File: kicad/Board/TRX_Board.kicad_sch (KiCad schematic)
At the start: 60 parts, among them J1 Conn_02x08_Odd_Even, J2 SMA, J3 Conn_01x03, J4 Conn_01x03, Q1 BSN20, Q2 BSN20, Q3 BSN20, U1 AP1117-33, U2 LM386, U3 DRA818U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

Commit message: Changed page information
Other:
- company: (none) -> digitalwire.ch
- title: (none) -> VHF-UHF TRX-Board
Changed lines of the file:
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@@
 (kicad_sch (version 20211123) (generator eeschema)
   (paper "A4")
+  (title_block
+    (title "VHF-UHF TRX-Board")
+    (date "2021-12-26")
+    (rev "V 1.0a")
+    (company "digitalwire.ch")
+  )
   (junction (at 205.74 72.39) (diameter 0) (color 0 0 0 0)
   )

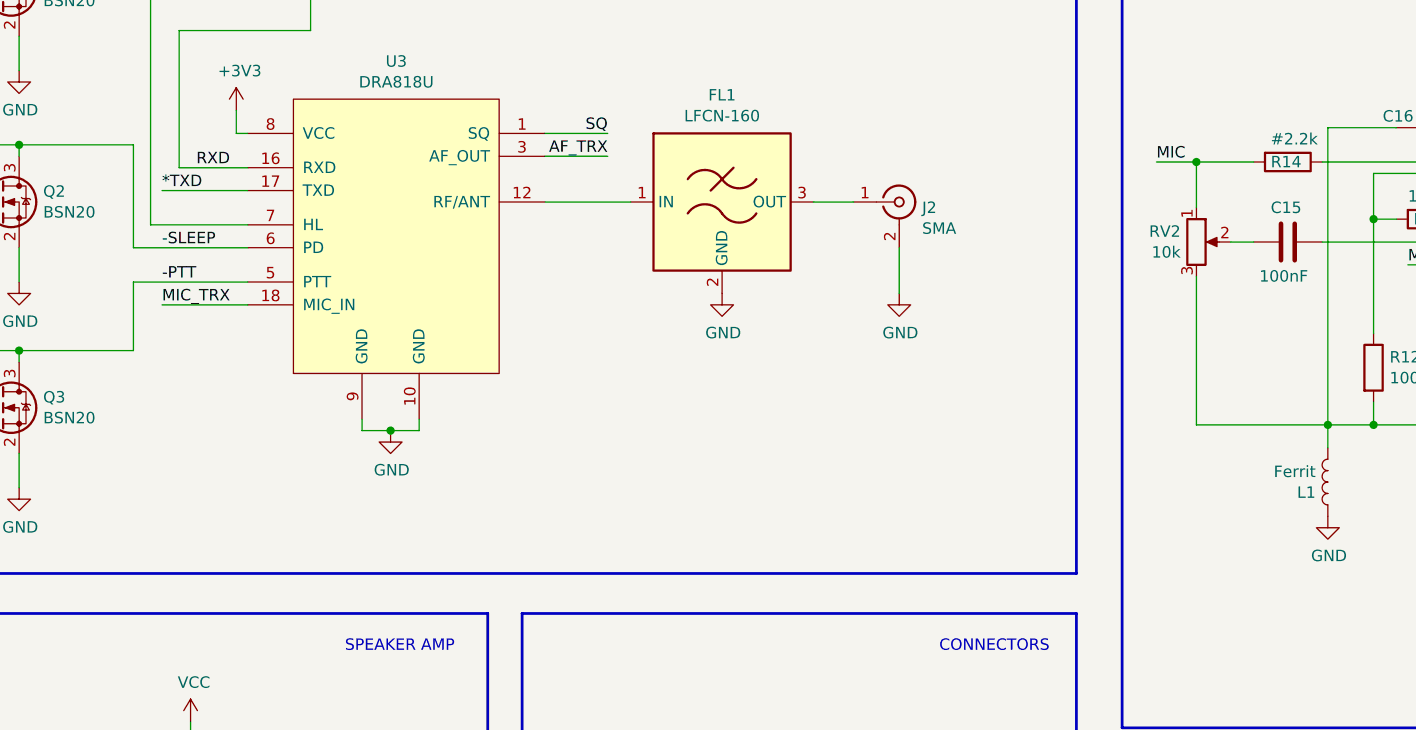
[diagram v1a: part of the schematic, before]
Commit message: Changed Mic Input
- Removed Poti near Mic
- Added Poti and jumper near the module
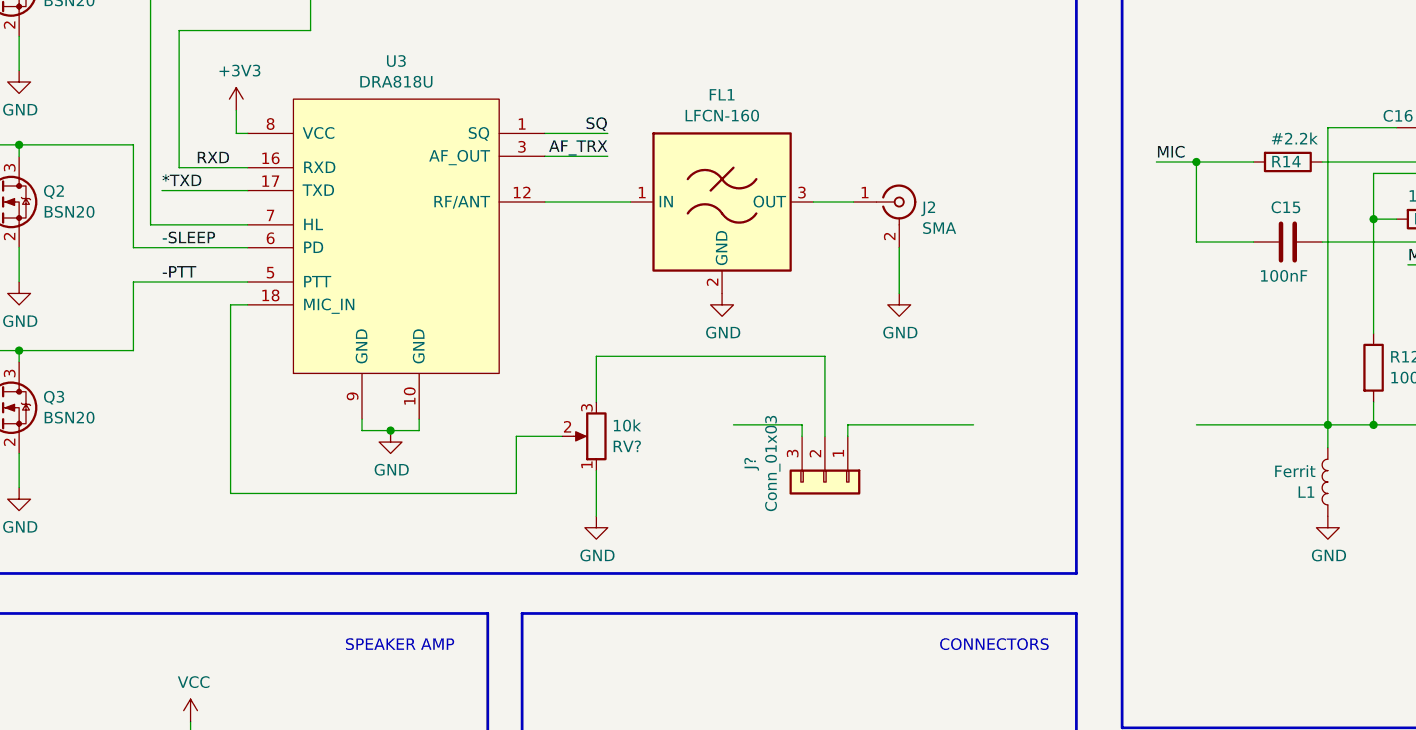
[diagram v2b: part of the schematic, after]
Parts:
- removed RV2: 10k, Potentiometer_SMD:Potentiometer_Vishay_TS53YL_Vertical, symbol Device:R_POT
- added J?: Conn_01x03, Connector_PinHeader_2.54mm:PinHeader_1x03_P2.54mm_Vertical, symbol Connector_Generic:Conn_01x03
- added RV?: 10k, Potentiometer_SMD:Potentiometer_Vishay_TS53YL_Vertical, symbol Device:R_POT
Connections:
- net GND: now also RV?.1
- net MIC: now also C15.2
- net MIC_TRX: no longer U3.18 (MIC_IN)
- new net: RV?.2, U3.18 (MIC_IN)
- new net: J?.2 (Pin_2), RV?.3
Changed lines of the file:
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@@
+    (stroke (width 0) (type default) (color 0 0 0 0))
+  )
+  (wire (pts (xy 137.16 73.66) (xy 137.16 72.39))
     (stroke (width 0) (type default) (color 0 0 0 0))
   )
@@
     (stroke (width 0) (type default) (color 0 0 0 0))
   )
+  (wire (pts (xy 68.58 59.055) (xy 68.58 80.01))
+    (stroke (width 0) (type default) (color 0 0 0 0))
+  )
   (wire (pts (xy 241.3 64.77) (xy 241.3 72.39))
+    (stroke (width 0) (type default) (color 0 0 0 0))
+  )
+  (wire (pts (xy 100.33 80.01) (xy 100.33 73.66))
     (stroke (width 0) (type default) (color 0 0 0 0))
   )
@@
     (stroke (width 0) (type default) (color 0 0 0 0))
   )
+  (wire (pts (xy 100.33 73.66) (xy 105.41 73.66))
+    (stroke (width 0) (type default) (color 0 0 0 0))
+  )
   (wire (pts (xy 70.485 46.355) (xy 60.96 46.355))
     (stroke (width 0) (type default) (color 0 0 0 0))
@@
     (stroke (width 0) (type default) (color 0 0 0 0))
   )
+  (wire (pts (xy 70.485 59.055) (xy 68.58 59.055))
+    (stroke (width 0) (type default) (color 0 0 0 0))
+  )
+  (wire (pts (xy 124.46 72.39) (xy 132.08 72.39))
+    (stroke (width 0) (type default) (color 0 0 0 0))
+  )
   (wire (pts (xy 41.275 171.45) (xy 41.275 167.005))
     (stroke (width 0) (type default) (color 0 0 0 0))
@@
   )
   (wire (pts (xy 64.135 141.605) (xy 76.835 141.605))
-    (stroke (width 0) (type default) (color 0 0 0 0))
-  )
-  (wire (pts (xy 70.485 59.055) (xy 60.96 59.055))
     (stroke (width 0) (type default) (color 0 0 0 0))
   )
@@
     (stroke (width 0.3048) (type default) (color 0 0 0 0))
   )
-  (wire (pts (xy 175.895 72.39) (xy 175.895 55.88))
-    (stroke (width 0) (type default) (color 0 0 0 0))
-  )
   (wire (pts (xy 57.785 64.135) (xy 45.085 64.135))
     (stroke (width 0) (type default) (color 0 0 0 0))
   )
-  (wire (pts (xy 179.705 52.07) (xy 182.245 52.07))
+  (wire (pts (xy 175.895 52.07) (xy 182.245 52.07))
     (stroke (width 0) (type default) (color 0 0 0 0))
   )
@@
     (stroke (width 0.3048) (type default) (color 0 0 0 0))
   )
+  (wire (pts (xy 132.08 73.66) (xy 132.08 72.39))
+    (stroke (width 0) (type default) (color 0 0 0 0))
+  )
   (wire (pts (xy 33.655 41.275) (xy 45.085 41.275))
     (stroke (width 0) (type default) (color 0 0 0 0))
   )
   (wire (pts (xy 215.9 72.39) (xy 205.74 72.39))
+    (stroke (width 0) (type default) (color 0 0 0 0))
+  )
+  (wire (pts (xy 134.62 64.77) (xy 134.62 73.66))
     (stroke (width 0) (type default) (color 0 0 0 0))
   )
@@
     (stroke (width 0.3048) (type default) (color 0 0 0 0))
   )
+  (wire (pts (xy 68.58 80.01) (xy 100.33 80.01))
+    (stroke (width 0) (type default) (color 0 0 0 0))
+  )
   (wire (pts (xy 265.43 72.39) (xy 254 72.39))
     (stroke (width 0) (type default) (color 0 0 0 0))
@@
     (stroke (width 0) (type default) (color 0 0 0 0))
   )
-  (wire (pts (xy 175.895 48.26) (xy 175.895 43.18))
+  (wire (pts (xy 175.895 43.18) (xy 175.895 52.07))
     (stroke (width 0) (type default) (color 0 0 0 0))
   )
@@
   )
   (wire (pts (xy 265.43 31.75) (xy 265.43 72.39))
+    (stroke (width 0) (type default) (color 0 0 0 0))
+  )
+  (wire (pts (xy 109.22 69.85) (xy 109.22 64.77))
     (stroke (width 0) (type default) (color 0 0 0 0))
   )
@@
     (stroke (width 0) (type default) (color 0 0 0 0))
   )
+  (wire (pts (xy 137.16 72.39) (xy 151.13 72.39))
+    (stroke (width 0) (type default) (color 0 0 0 0))
+  )
   (wire (pts (xy 223.52 128.27) (xy 223.52 125.095))
     (stroke (width 0) (type default) (color 0 0 0 0))
@@
     (stroke (width 0) (type default) (color 0 0 0 0))
   )
+  (wire (pts (xy 109.22 77.47) (xy 109.22 82.55))
+    (stroke (width 0) (type default) (color 0 0 0 0))
+  )
   (wire (pts (xy 35.56 48.895) (xy 35.56 47.625))
     (stroke (width 0) (type default) (color 0 0 0 0))
@@
     (stroke (width 0) (type default) (color 0 0 0 0))
   )
+  (wire (pts (xy 109.22 64.77) (xy 134.62 64.77))
+    (stroke (width 0) (type default) (color 0 0 0 0))
+  )
   (wire (pts (xy 33.02 64.135) (xy 45.085 64.135))
     (stroke (width 0) (type default) (color 0 0 0 0))
@@
   (label "SPKR" (at 95.25 118.11 180)
     (effects (font (size 1.27 1.27)) (justify right bottom))
-  )
-  (label "MIC_TRX" (at 60.96 59.055 0)
-    (effects (font (size 1.27 1.27)) (justify left bottom))
   )
   (label "*SLEEP" (at 19.05 47.625 0)
@@
     (pin "2")
   )
-  (symbol (lib_id "Device:R_POT") (at 175.895 52.07 0) (unit 1)
-    (in_bom yes) (on_board yes)
-    (property "Reference" "RV2" (id 0) (at 174.1424 50.9016 0)
-      (effects (font (size 1.27 1.27)) (justify right))
-    )
-    (property "Value" "10k" (id 1) (at 174.1424 53.213 0)
-      (effects (font (size 1.27 1.27)) (justify right))
-    )
-    (property "Footprint" "Potentiometer_SMD:Potentiometer_Vishay_TS53YL_Vertical" (id 2) (at 175.895 52.07 0)
-      (effects (font (size 1.27 1.27)) hide)
-    )
-    (property "Datasheet" "https://www.farnell.com/datasheets/2243510.pdf" (id 3) (at 175.895 52.07 0)
-      (effects (font (size 1.27 1.27)) hide)
-    )
-    (pin "1")
-    (pin "2")
-    (pin "3")
-  )
   (symbol (lib_id "Connector_Generic:Conn_01x03") (at 252.73 93.345 180) (unit 1)
     (in_bom yes) (on_board yes)
@@
     (pin "1")
   )
+  (symbol (lib_id "Device:R_POT") (at 109.22 73.66 180) (unit 1)
+    (in_bom yes) (on_board yes)
+    (property "Reference" "RV?" (id 0) (at 110.9726 74.8284 0)
+      (effects (font (size 1.27 1.27)) (justify right))
+    )
+    (property "Value" "10k" (id 1) (at 110.9726 72.517 0)
+      (effects (font (size 1.27 1.27)) (justify right))
+    )
+    (property "Footprint" "Potentiometer_SMD:Potentiometer_Vishay_TS53YL_Vertical" (id 2) (at 109.22 73.66 0)
+      (effects (font (size 1.27 1.27)) hide)
+    )
+    (property "Datasheet" "https://www.farnell.com/datasheets/2243510.pdf" (id 3) (at 109.22 73.66 0)
+      (effects (font (size 1.27 1.27)) hide)
+    )
+    (pin "1")
+    (pin "2")
+    (pin "3")
+  )
+  (symbol (lib_id "Connector_Generic:Conn_01x03") (at 134.62 78.74 270) (unit 1)
+    (in_bom yes) (on_board yes)
+    (property "Reference" "J?" (id 0) (at 126.365 76.6572 0))
+    (property "Value" "Conn_01x03" (id 1) (at 128.6764 76.6572 0))
+    (property "Footprint" "Connector_PinHeader_2.54mm:PinHeader_1x03_P2.54mm_Vertical" (id 2) (at 134.62 78.74 0)
+      (effects (font (size 1.27 1.27)) hide)
+    )
+    (property "Datasheet" "~" (id 3) (at 134.62 78.74 0)
+      (effects (font (size 1.27 1.27)) hide)
+    )
+    (pin "1")
+    (pin "2")
+    (pin "3")
+  )
+  (symbol (lib_id "power:GND") (at 109.22 82.55 0) (unit 1)
+    (in_bom yes) (on_board yes)
+    (property "Reference" "#PWR?" (id 0) (at 109.22 88.9 0)
+      (effects (font (size 1.27 1.27)) hide)
+    )
+    (property "Value" "GND" (id 1) (at 109.347 86.9442 0))
+    (property "Footprint" "" (id 2) (at 109.22 82.55 0)
+      (effects (font (size 1.27 1.27)) hide)
+    )
+    (property "Datasheet" "" (id 3) (at 109.22 82.55 0)
+      (effects (font (size 1.27 1.27)) hide)
+    )
+    (pin "1")
+  )
   (sheet_instances
     (path "/" (page "1"))
@@
       (reference "#PWR0123") (unit 1) (value "+3V3") (footprint "")
     )
+    (path "/e6dfebc1-3066-4114-850c-c1ad4d514bbe"
+      (reference "#PWR?") (unit 1) (value "GND") (footprint "")
+    )
     (path "/00000000-0000-0000-0000-000061adb17e"
       (reference "C1") (unit 1) (value "1uF") (footprint "Capacitor_SMD:C_0805_2012Metric")
@@
       (reference "J4") (unit 1) (value "Conn_01x03") (footprint "Connector_PinHeader_2.54mm:PinHeader_1x03_P2.54mm_Vertical")
     )
+    (path "/ad88d716-a3fc-4190-9eea-4afb2b173e02"
+      (reference "J?") (unit 1) (value "Conn_01x03") (footprint "Connector_PinHeader_2.54mm:PinHeader_1x03_P2.54mm_Vertical")
+    )
     (path "/00000000-0000-0000-0000-000061bd53ee"
       (reference "L1") (unit 1) (value "Ferrit") (footprint "Resistor_SMD:R_0805_2012Metric_Pad1.20x1.40mm_HandSolder")
@@
       (reference "RV1") (unit 1) (value "10k") (footprint "Potentiometer_SMD:Potentiometer_Vishay_TS53YL_Vertical")
     )
-    (path "/00000000-0000-0000-0000-000061bf5408"
-      (reference "RV2") (unit 1) (value "10k") (footprint "Potentiometer_SMD:Potentiometer_Vishay_TS53YL_Vertical")
+    (path "/517aeb5d-8eab-4421-9d39-bacc4bae273d"
+      (reference "RV?") (unit 1) (value "10k") (footprint "Potentiometer_SMD:Potentiometer_Vishay_TS53YL_Vertical")
     )
     (path "/00000000-0000-0000-0000-000061a2a793"

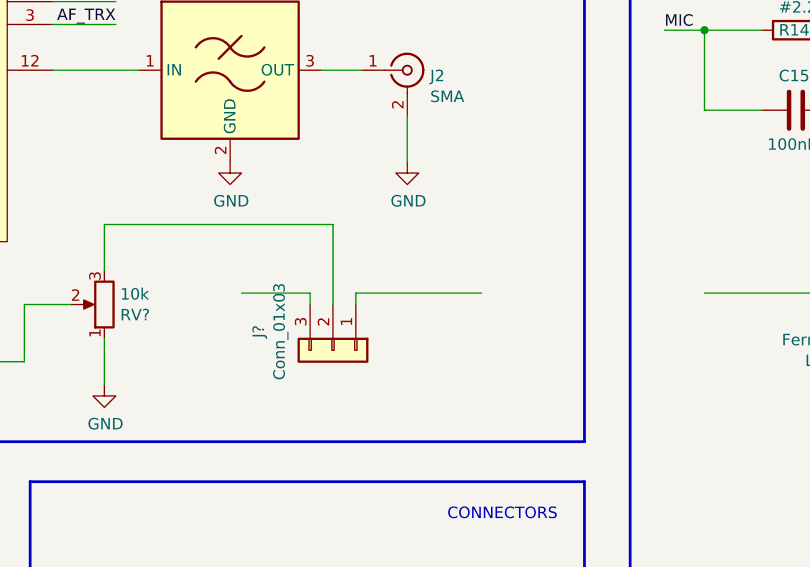
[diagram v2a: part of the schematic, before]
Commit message: Added Labels
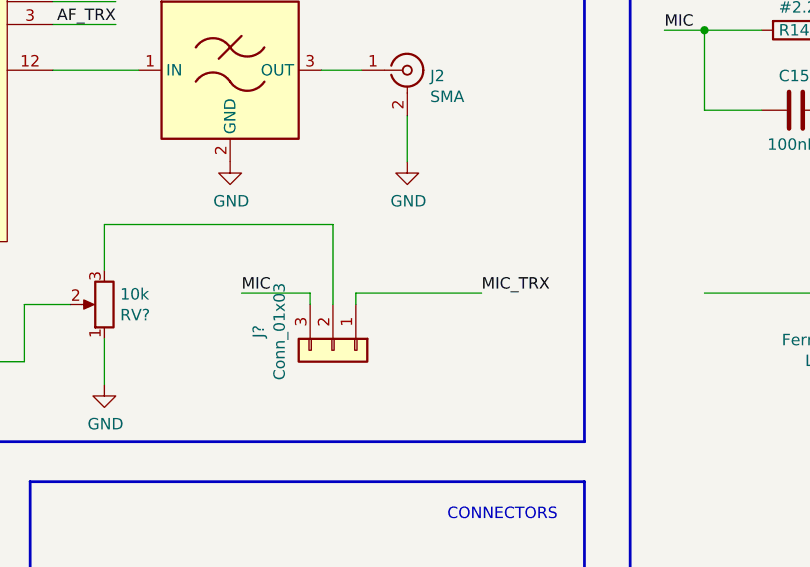
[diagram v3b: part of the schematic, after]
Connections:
- net MIC: now also J?.3 (Pin_3)
- net MIC_TRX: now also J?.1 (Pin_1)
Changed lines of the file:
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@@
+    (effects (font (size 1.27 1.27)) (justify left bottom))
+  )
+  (label "MIC" (at 124.46 72.39 0)
     (effects (font (size 1.27 1.27)) (justify left bottom))
   )
@@
     (effects (font (size 1.27 1.27)) (justify right bottom))
   )
+  (label "MIC_TRX" (at 151.13 72.39 0)
+    (effects (font (size 1.27 1.27)) (justify left bottom))
+  )
   (label "RXD" (at 179.07 152.4 0)

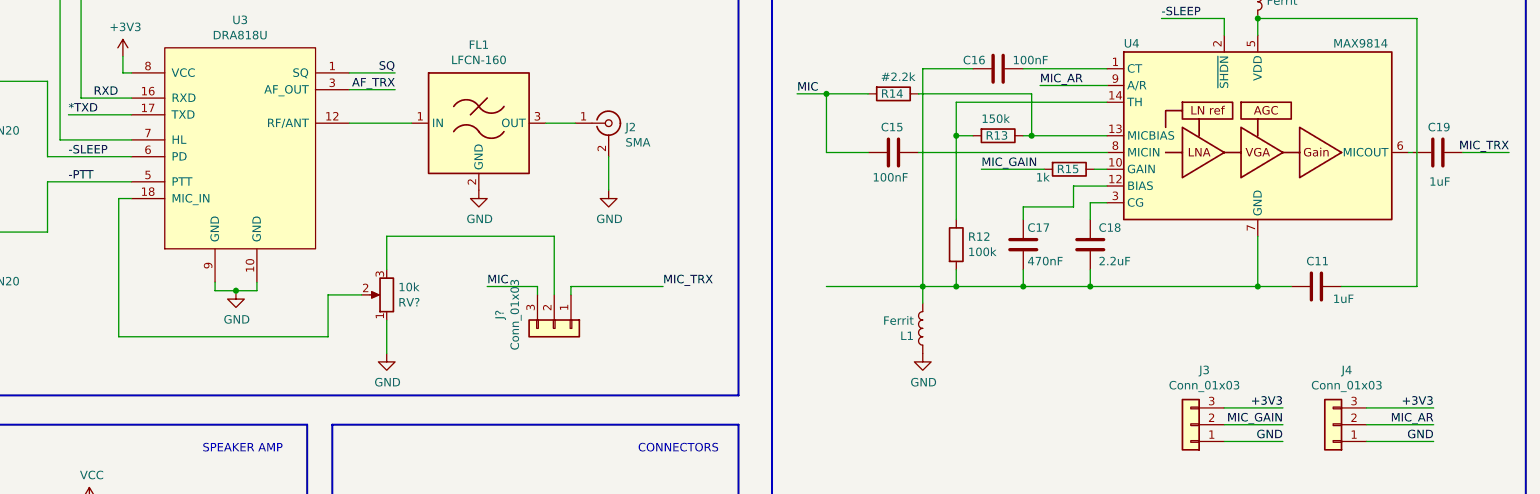
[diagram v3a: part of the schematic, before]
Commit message: Changed position of C on MICOUT of MAX...
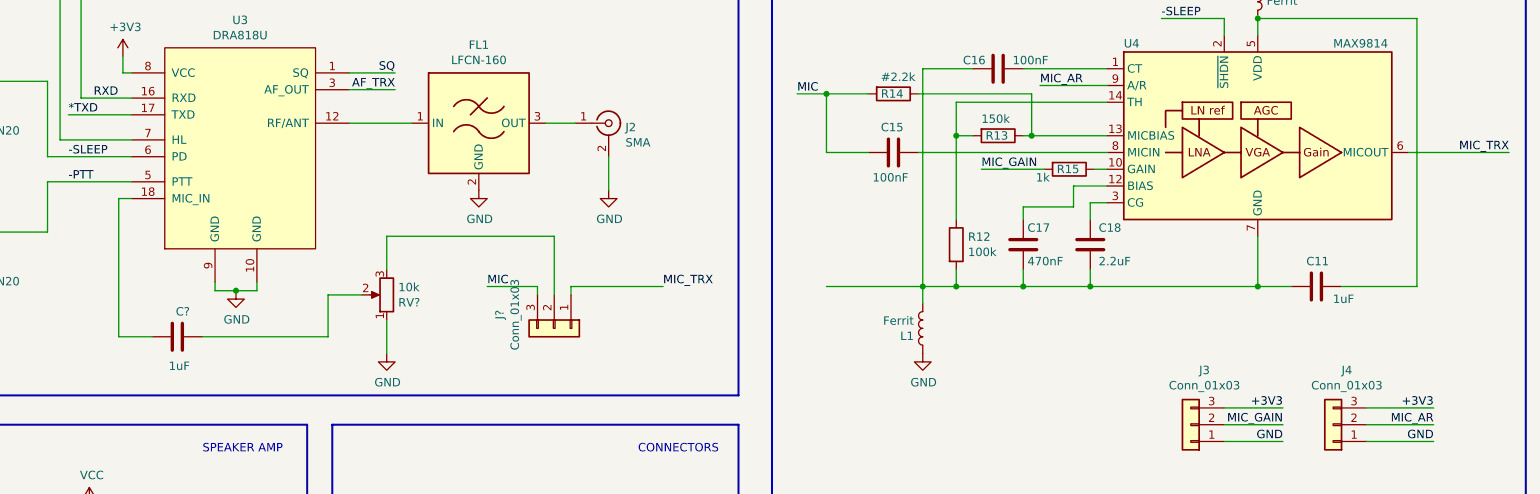
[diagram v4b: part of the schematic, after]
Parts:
- removed C19: 1uF, Capacitor_SMD:C_0805_2012Metric, symbol Device:C
- added C?: 1uF, Capacitor_SMD:C_0805_2012Metric, symbol Device:C
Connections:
- net MIC_TRX: now also U4.6 (MICOUT)
- net at U3.18 (MIC_IN): now also C?.1; no longer RV?.2
- new net: C?.2, RV?.2
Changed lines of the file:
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@@
-    (stroke (width 0) (type default) (color 0 0 0 0))
-  )
-  (wire (pts (xy 264.16 52.07) (xy 264.795 52.07))
     (stroke (width 0) (type default) (color 0 0 0 0))
   )
@@
   )
   (wire (pts (xy 186.69 128.27) (xy 186.69 125.095))
+    (stroke (width 0) (type default) (color 0 0 0 0))
+  )
+  (wire (pts (xy 81.28 80.01) (xy 100.33 80.01))
     (stroke (width 0) (type default) (color 0 0 0 0))
   )
@@
     (stroke (width 0) (type default) (color 0 0 0 0))
   )
-  (wire (pts (xy 272.415 52.07) (xy 279.4 52.07))
+  (wire (pts (xy 264.16 52.07) (xy 279.4 52.07))
     (stroke (width 0) (type default) (color 0 0 0 0))
   )
@@
     (stroke (width 0.3048) (type default) (color 0 0 0 0))
   )
-  (wire (pts (xy 68.58 80.01) (xy 100.33 80.01))
+  (wire (pts (xy 68.58 80.01) (xy 73.66 80.01))
     (stroke (width 0) (type default) (color 0 0 0 0))
   )
@@
     (pin "2")
   )
-  (symbol (lib_id "Device:C") (at 268.605 52.07 90) (unit 1)
-    (in_bom yes) (on_board yes)
-    (property "Reference" "C19" (id 0) (at 270.51 48.26 90)
-      (effects (font (size 1.27 1.27)) (justify left))
-    )
-    (property "Value" "1uF" (id 1) (at 270.51 56.515 90)
-      (effects (font (size 1.27 1.27)) (justify left))
-    )
-    (property "Footprint" "Capacitor_SMD:C_0805_2012Metric" (id 2) (at 272.415 51.1048 0)
-      (effects (font (size 1.27 1.27)) hide)
-    )
-    (property "Datasheet" "https://datasheet.lcsc.com/lcsc/1810191216_Samsung-Electro-Mechanics-CL21B105KBFNNNE_C28323.pdf" (id 3) (at 268.605 52.07 0)
-      (effects (font (size 1.27 1.27)) hide)
-    )
-    (property "LCSC" "C28323" (id 4) (at 268.605 52.07 0)
-      (effects (font (size 1.27 1.27)) hide)
-    )
-    (pin "1")
-    (pin "2")
-  )
   (symbol (lib_id "Device:R") (at 195.58 66.04 0) (unit 1)
     (in_bom yes) (on_board yes)
@@
     (pin "1")
   )
+  (symbol (lib_id "Device:C") (at 77.47 80.01 90) (unit 1)
+    (in_bom yes) (on_board yes)
+    (property "Reference" "C?" (id 0) (at 79.375 76.2 90)
+      (effects (font (size 1.27 1.27)) (justify left))
+    )
+    (property "Value" "1uF" (id 1) (at 79.375 84.455 90)
+      (effects (font (size 1.27 1.27)) (justify left))
+    )
+    (property "Footprint" "Capacitor_SMD:C_0805_2012Metric" (id 2) (at 81.28 79.0448 0)
+      (effects (font (size 1.27 1.27)) hide)
+    )
+    (property "Datasheet" "https://datasheet.lcsc.com/lcsc/1810191216_Samsung-Electro-Mechanics-CL21B105KBFNNNE_C28323.pdf" (id 3) (at 77.47 80.01 0)
+      (effects (font (size 1.27 1.27)) hide)
+    )
+    (property "LCSC" "C28323" (id 4) (at 77.47 80.01 0)
+      (effects (font (size 1.27 1.27)) hide)
+    )
+    (pin "1")
+    (pin "2")
+  )
   (symbol (lib_id "Device:R_POT") (at 109.22 73.66 180) (unit 1)
     (in_bom yes) (on_board yes)
@@
       (reference "C18") (unit 1) (value "2.2uF") (footprint "Capacitor_SMD:C_0805_2012Metric")
     )
-    (path "/00000000-0000-0000-0000-000061a9d8d3"
-      (reference "C19") (unit 1) (value "1uF") (footprint "Capacitor_SMD:C_0805_2012Metric")
+    (path "/33d9a8cf-31ed-405a-9422-9faebf8878bc"
+      (reference "C?") (unit 1) (value "1uF") (footprint "Capacitor_SMD:C_0805_2012Metric")
     )
     (path "/00000000-0000-0000-0000-000061c0b6bb"
